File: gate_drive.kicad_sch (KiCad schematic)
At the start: 111 parts, among them U1 EG2131, U10 EG2131, U12 EG2131, U2 EG2131, U3 LM358, U4 EG2131, U5 EG2131, U8 LM358

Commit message: Updated PCB design based on feedback. Added thermistors, mounting holes. This design has better current carrying capacity. gerber folder may not be perfect right now.
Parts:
- removed C13: HIGHCURRENTPAD2, RP2040_minimal:PAD_12GA_WIRE, symbol Connector_Generic:Conn_01x01
- added M2C1: HIGHCURRENTPAD2, RP2040_minimal:PAD_12GA_WIRE, symbol Connector_Generic:Conn_01x01
- added TP1: TestPoint, symbol Connector:TestPoint
- R20, R22, R24, R26, R3, R4, R54, R55, R56, R57: value 22R -> 10.2R; LCSC C23345 -> C22773
- renumbered A1 to M1A1, B1 to M1B1, C12 to M1C1, A2 to M2A1, B2 to M2B1
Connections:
- net M2C: now also M2C1.1 (Pin_1)
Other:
- moved on the sheet: M2A1
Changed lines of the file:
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@@
     (stroke (width 0) (type default) (color 0 0 0 0))
   )
-  (wire (pts (xy 311.15 186.055) (xy 314.96 186.055))
+  (wire (pts (xy 311.15 186.055) (xy 316.23 186.055))
     (stroke (width 0) (type default) (color 0 0 0 0))
   )
@@
     (stroke (width 0) (type default) (color 0 0 0 0))
   )
-  (wire (pts (xy 120.015 182.88) (xy 123.825 182.88))
+  (wire (pts (xy 120.015 182.88) (xy 125.73 182.88))
     (stroke (width 0) (type default) (color 0 0 0 0))
   )
@@
     (pin "8")
   )
-  (symbol (lib_id "Connector_Generic:Conn_01x01") (at 128.905 182.88 0) (unit 1)
-    (in_bom no) (on_board yes)
-    (property "Reference" "C13" (id 0) (at 127.381 181.1274 0)
-      (effects (font (size 1.27 1.27)) (justify left bottom))
-    )
-    (property "Value" "HIGHCURRENTPAD2" (id 1) (at 128.651 185.674 0)
-      (effects (font (size 1.651 1.651)) (justify left top) hide)
-    )
-    (property "Footprint" "RP2040_minimal:PAD_12GA_WIRE" (id 2) (at 128.905 182.88 0)
-      (effects (font (size 1.27 1.27)) hide)
-    )
-    (property "Datasheet" "~" (id 3) (at 128.905 182.88 0)
-      (effects (font (size 1.27 1.27)) hide)
-    )
-    (pin "1")
-  )
   (symbol (lib_id "MotorController:TAYLOR_RESISTOR") (at 292.1 182.245 0) (unit 1)
     (in_bom yes) (on_board yes)
@@
       (effects (font (size 1.778 1.778)) (justify left bottom))
     )
-    (property "Value" "22R" (id 1) (at 288.29 185.547 0)
+    (property "Value" "10.2R" (id 1) (at 288.29 185.547 0)
       (effects (font (size 1.778 1.778)) (justify left bottom))
     )
@@
       (effects (font (size 1.27 1.27)) hide)
     )
-    (property "LCSC" "C23345" (id 4) (at 292.1 182.245 0)
+    (property "LCSC" "C22773" (id 4) (at 292.1 182.245 0)
       (effects (font (size 1.27 1.27)) hide)
     )
@@
   (symbol (lib_id "Connector_Generic:Conn_01x01") (at 211.455 57.15 0) (unit 1)
     (in_bom no) (on_board yes)
-    (property "Reference" "B1" (id 0) (at 209.931 55.3974 0)
+    (property "Reference" "M1B1" (id 0) (at 209.931 55.3974 0)
       (effects (font (size 1.27 1.27)) (justify left bottom))
     )
@@
     (pin "2")
   )
-  (symbol (lib_id "Connector_Generic:Conn_01x01") (at 320.04 186.055 0) (unit 1)
+  (symbol (lib_id "Connector_Generic:Conn_01x01") (at 321.31 186.055 0) (unit 1)
     (in_bom no) (on_board yes)
-    (property "Reference" "A2" (id 0) (at 318.516 184.3024 0)
+    (property "Reference" "M2A1" (id 0) (at 319.786 184.3024 0)
       (effects (font (size 1.27 1.27)) (justify left bottom))
     )
-    (property "Value" "HIGHCURRENTPAD2" (id 1) (at 319.786 188.849 0)
+    (property "Value" "HIGHCURRENTPAD2" (id 1) (at 321.056 188.849 0)
       (effects (font (size 1.651 1.651)) (justify left top) hide)
     )
-    (property "Footprint" "RP2040_minimal:PAD_12GA_WIRE" (id 2) (at 320.04 186.055 0)
+    (property "Footprint" "RP2040_minimal:PAD_12GA_WIRE" (id 2) (at 321.31 186.055 0)
       (effects (font (size 1.27 1.27)) hide)
     )
-    (property "Datasheet" "~" (id 3) (at 320.04 186.055 0)
+    (property "Datasheet" "~" (id 3) (at 321.31 186.055 0)
       (effects (font (size 1.27 1.27)) hide)
     )
@@
       (effects (font (size 1.778 1.778)) (justify left bottom))
     )
-    (property "Value" "22R" (id 1) (at 270.51 57.277 0)
+    (property "Value" "10.2R" (id 1) (at 270.51 57.277 0)
       (effects (font (size 1.778 1.778)) (justify left bottom))
     )
@@
       (effects (font (size 1.27 1.27)) hide)
     )
-    (property "LCSC" "C23345" (id 4) (at 274.32 53.975 0)
+    (property "LCSC" "C22773" (id 4) (at 274.32 53.975 0)
       (effects (font (size 1.27 1.27)) hide)
     )
@@
   (symbol (lib_id "Connector_Generic:Conn_01x01") (at 123.19 56.515 0) (unit 1)
     (in_bom no) (on_board yes)
-    (property "Reference" "C12" (id 0) (at 121.666 54.7624 0)
+    (property "Reference" "M1C1" (id 0) (at 121.666 54.7624 0)
       (effects (font (size 1.27 1.27)) (justify left bottom))
     )
@@
   (symbol (lib_id "Connector_Generic:Conn_01x01") (at 222.25 186.055 0) (unit 1)
     (in_bom no) (on_board yes)
-    (property "Reference" "B2" (id 0) (at 220.726 184.3024 0)
+    (property "Reference" "M2B1" (id 0) (at 220.726 184.3024 0)
       (effects (font (size 1.27 1.27)) (justify left bottom))
     )
@@
       (effects (font (size 1.778 1.778)) (justify left bottom))
     )
-    (property "Value" "22R" (id 1) (at 179.705 56.642 0)
+    (property "Value" "10.2R" (id 1) (at 179.705 56.642 0)
       (effects (font (size 1.778 1.778)) (justify left bottom))
     )
@@
       (effects (font (size 1.27 1.27)) hide)
     )
-    (property "LCSC" "C23345" (id 4) (at 183.515 53.34 0)
+    (property "LCSC" "C22773" (id 4) (at 183.515 53.34 0)
       (effects (font (size 1.27 1.27)) hide)
     )
@@
     (pin "2")
   )
+  (symbol (lib_id "Connector:TestPoint") (at -6.35 -104.14 0) (unit 1)
+    (in_bom yes) (on_board yes) (fields_autoplaced)
+    (property "Reference" "TP1" (id 0) (at -2.54 -108.7121 0)
+      (effects (font (size 1.27 1.27)) (justify left))
+    )
+    (property "Value" "TestPoint" (id 1) (at -2.54 -106.1721 0)
+      (effects (font (size 1.27 1.27)) (justify left))
+    )
+    (property "Footprint" "" (id 2) (at -1.27 -104.14 0)
+      (effects (font (size 1.27 1.27)) hide)
+    )
+    (property "Datasheet" "~" (id 3) (at -1.27 -104.14 0)
+      (effects (font (size 1.27 1.27)) hide)
+    )
+    (pin "1")
+  )
   (symbol (lib_id "Device:D") (at 185.42 164.465 180) (unit 1)
     (in_bom yes) (on_board yes) (fields_autoplaced)
@@
       (effects (font (size 1.778 1.778)) (justify left bottom))
     )
-    (property "Value" "22R" (id 1) (at 97.155 182.372 0)
+    (property "Value" "10.2R" (id 1) (at 97.155 182.372 0)
       (effects (font (size 1.778 1.778)) (justify left bottom))
     )
@@
       (effects (font (size 1.27 1.27)) hide)
     )
-    (property "LCSC" "C23345" (id 4) (at 100.965 179.07 0)
+    (property "LCSC" "C22773" (id 4) (at 100.965 179.07 0)
       (effects (font (size 1.27 1.27)) hide)
     )
@@
   (symbol (lib_id "Connector_Generic:Conn_01x01") (at 302.26 57.785 0) (unit 1)
     (in_bom no) (on_board yes)
-    (property "Reference" "A1" (id 0) (at 300.736 56.0324 0)
+    (property "Reference" "M1A1" (id 0) (at 300.736 56.0324 0)
       (effects (font (size 1.27 1.27)) (justify left bottom))
     )
@@
       (effects (font (size 1.778 1.778)) (justify left bottom))
     )
-    (property "Value" "22R" (id 1) (at 270.51 71.247 0)
+    (property "Value" "10.2R" (id 1) (at 270.51 71.247 0)
       (effects (font (size 1.778 1.778)) (justify left bottom))
     )
@@
       (effects (font (size 1.27 1.27)) hide)
     )
-    (property "LCSC" "C23345" (id 4) (at 274.32 67.945 0)
+    (property "LCSC" "C22773" (id 4) (at 274.32 67.945 0)
       (effects (font (size 1.27 1.27)) hide)
     )
@@
       (effects (font (size 1.778 1.778)) (justify left bottom))
     )
-    (property "Value" "22R" (id 1) (at 288.29 199.517 0)
+    (property "Value" "10.2R" (id 1) (at 288.29 199.517 0)
       (effects (font (size 1.778 1.778)) (justify left bottom))
     )
@@
       (effects (font (size 1.27 1.27)) hide)
     )
-    (property "LCSC" "C23345" (id 4) (at 292.1 196.215 0)
+    (property "LCSC" "C22773" (id 4) (at 292.1 196.215 0)
       (effects (font (size 1.27 1.27)) hide)
     )
@@
       (effects (font (size 1.778 1.778)) (justify left bottom))
     )
-    (property "Value" "22R" (id 1) (at 190.5 199.517 0)
+    (property "Value" "10.2R" (id 1) (at 190.5 199.517 0)
       (effects (font (size 1.778 1.778)) (justify left bottom))
     )
@@
       (effects (font (size 1.27 1.27)) hide)
     )
-    (property "LCSC" "C23345" (id 4) (at 194.31 196.215 0)
+    (property "LCSC" "C22773" (id 4) (at 194.31 196.215 0)
       (effects (font (size 1.27 1.27)) hide)
     )
@@
       (effects (font (size 1.778 1.778)) (justify left bottom))
     )
-    (property "Value" "22R" (id 1) (at 97.155 196.342 0)
+    (property "Value" "10.2R" (id 1) (at 97.155 196.342 0)
       (effects (font (size 1.778 1.778)) (justify left bottom))
     )
@@
       (effects (font (size 1.27 1.27)) hide)
     )
-    (property "LCSC" "C23345" (id 4) (at 100.965 193.04 0)
+    (property "LCSC" "C22773" (id 4) (at 100.965 193.04 0)
       (effects (font (size 1.27 1.27)) hide)
     )
@@
       (effects (font (size 1.778 1.778)) (justify left bottom))
     )
-    (property "Value" "22R" (id 1) (at 190.5 185.547 0)
+    (property "Value" "10.2R" (id 1) (at 190.5 185.547 0)
       (effects (font (size 1.778 1.778)) (justify left bottom))
     )
@@
       (effects (font (size 1.27 1.27)) hide)
     )
-    (property "LCSC" "C23345" (id 4) (at 194.31 182.245 0)
+    (property "LCSC" "C22773" (id 4) (at 194.31 182.245 0)
       (effects (font (size 1.27 1.27)) hide)
     )
@@
       (effects (font (size 1.778 1.778)) (justify left bottom))
     )
-    (property "Value" "22R" (id 1) (at 179.705 70.612 0)
+    (property "Value" "10.2R" (id 1) (at 179.705 70.612 0)
       (effects (font (size 1.778 1.778)) (justify left bottom))
     )
@@
       (effects (font (size 1.27 1.27)) hide)
     )
-    (property "LCSC" "C23345" (id 4) (at 183.515 67.31 0)
+    (property "LCSC" "C22773" (id 4) (at 183.515 67.31 0)
       (effects (font (size 1.27 1.27)) hide)
     )
@@
     (pin "8")
   )
+  (symbol (lib_id "Connector_Generic:Conn_01x01") (at 130.81 182.88 0) (unit 1)
+    (in_bom no) (on_board yes)
+    (property "Reference" "M2C1" (id 0) (at 129.286 181.1274 0)
+      (effects (font (size 1.27 1.27)) (justify left bottom))
+    )
+    (property "Value" "HIGHCURRENTPAD2" (id 1) (at 130.556 185.674 0)
+      (effects (font (size 1.651 1.651)) (justify left top) hide)
+    )
+    (property "Footprint" "RP2040_minimal:PAD_12GA_WIRE" (id 2) (at 130.81 182.88 0)
+      (effects (font (size 1.27 1.27)) hide)
+    )
+    (property "Datasheet" "~" (id 3) (at 130.81 182.88 0)
+      (effects (font (size 1.27 1.27)) hide)
+    )
+    (pin "1")
+  )
 )

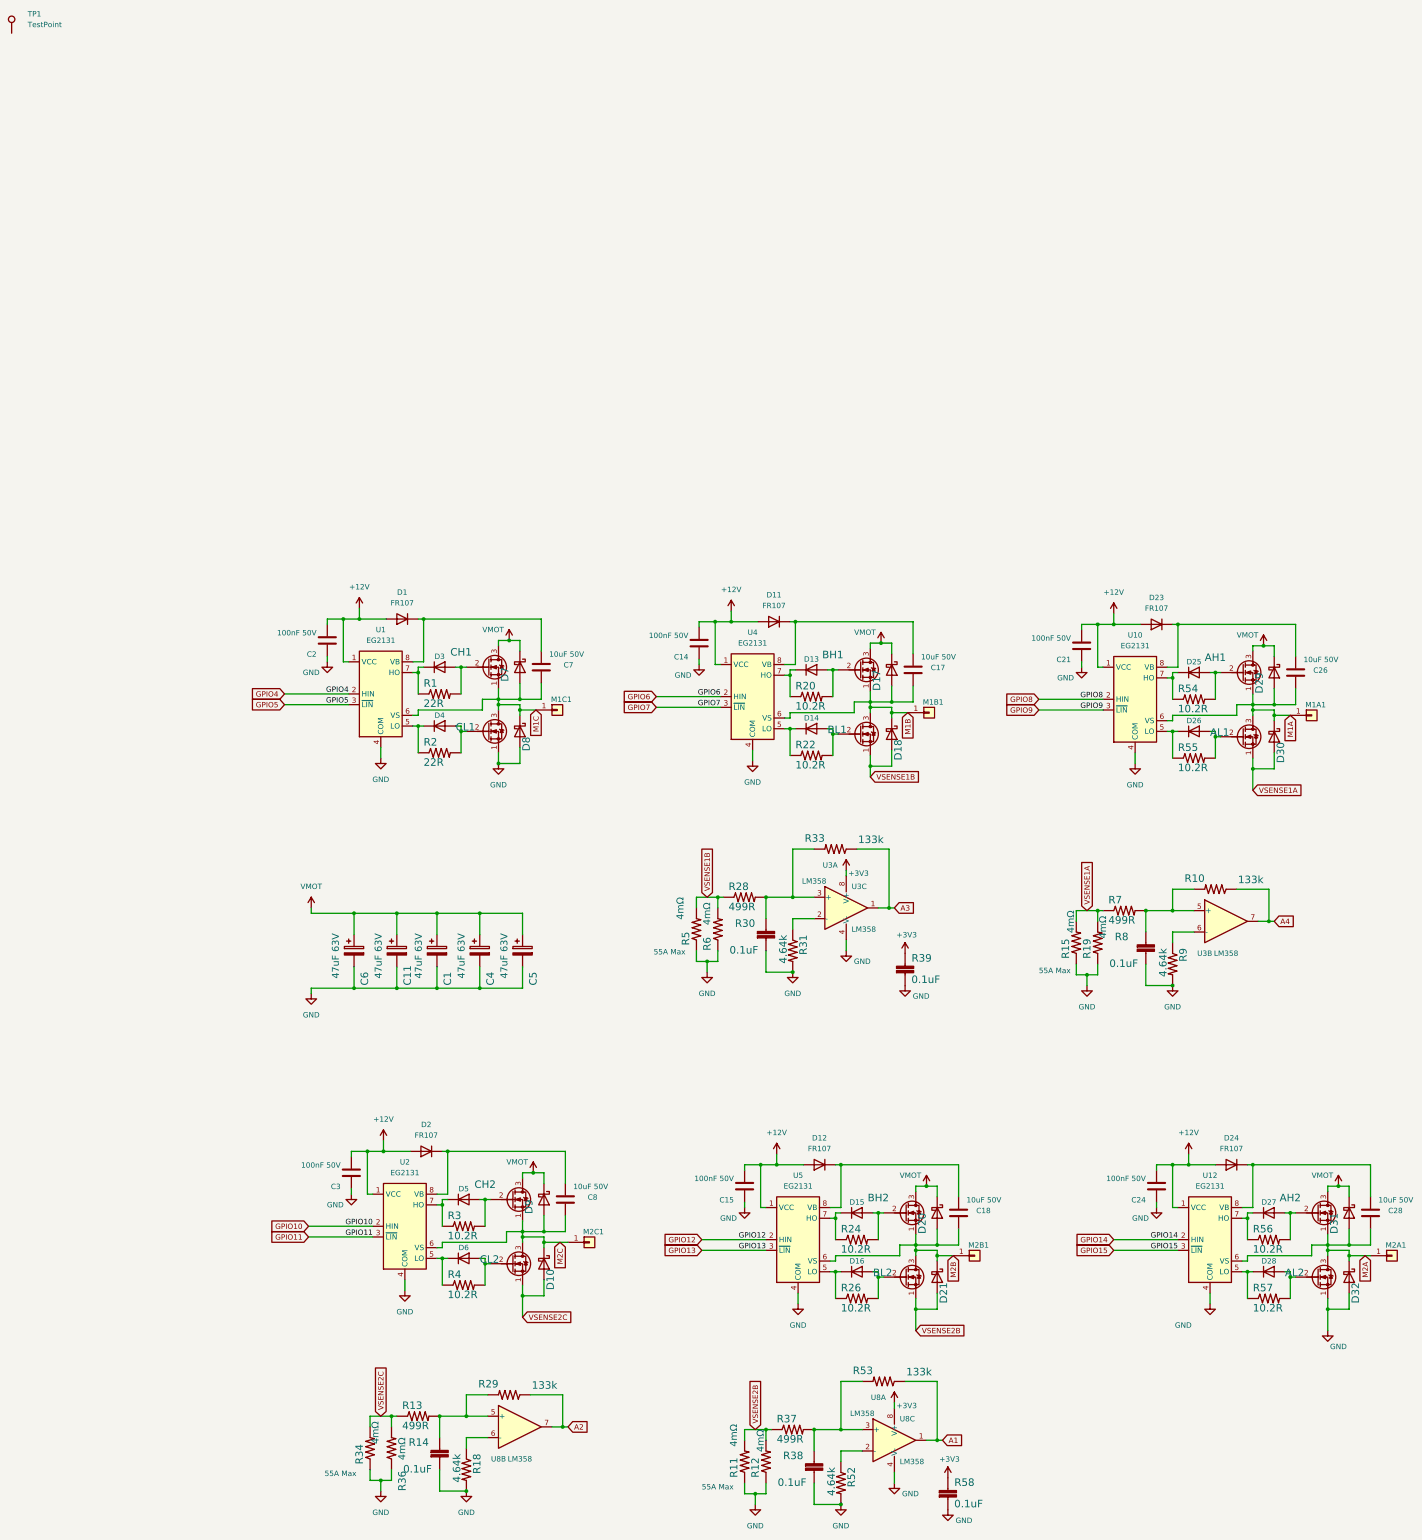
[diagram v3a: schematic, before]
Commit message: Additional updates to clean up power and capacitance on buck circuit.
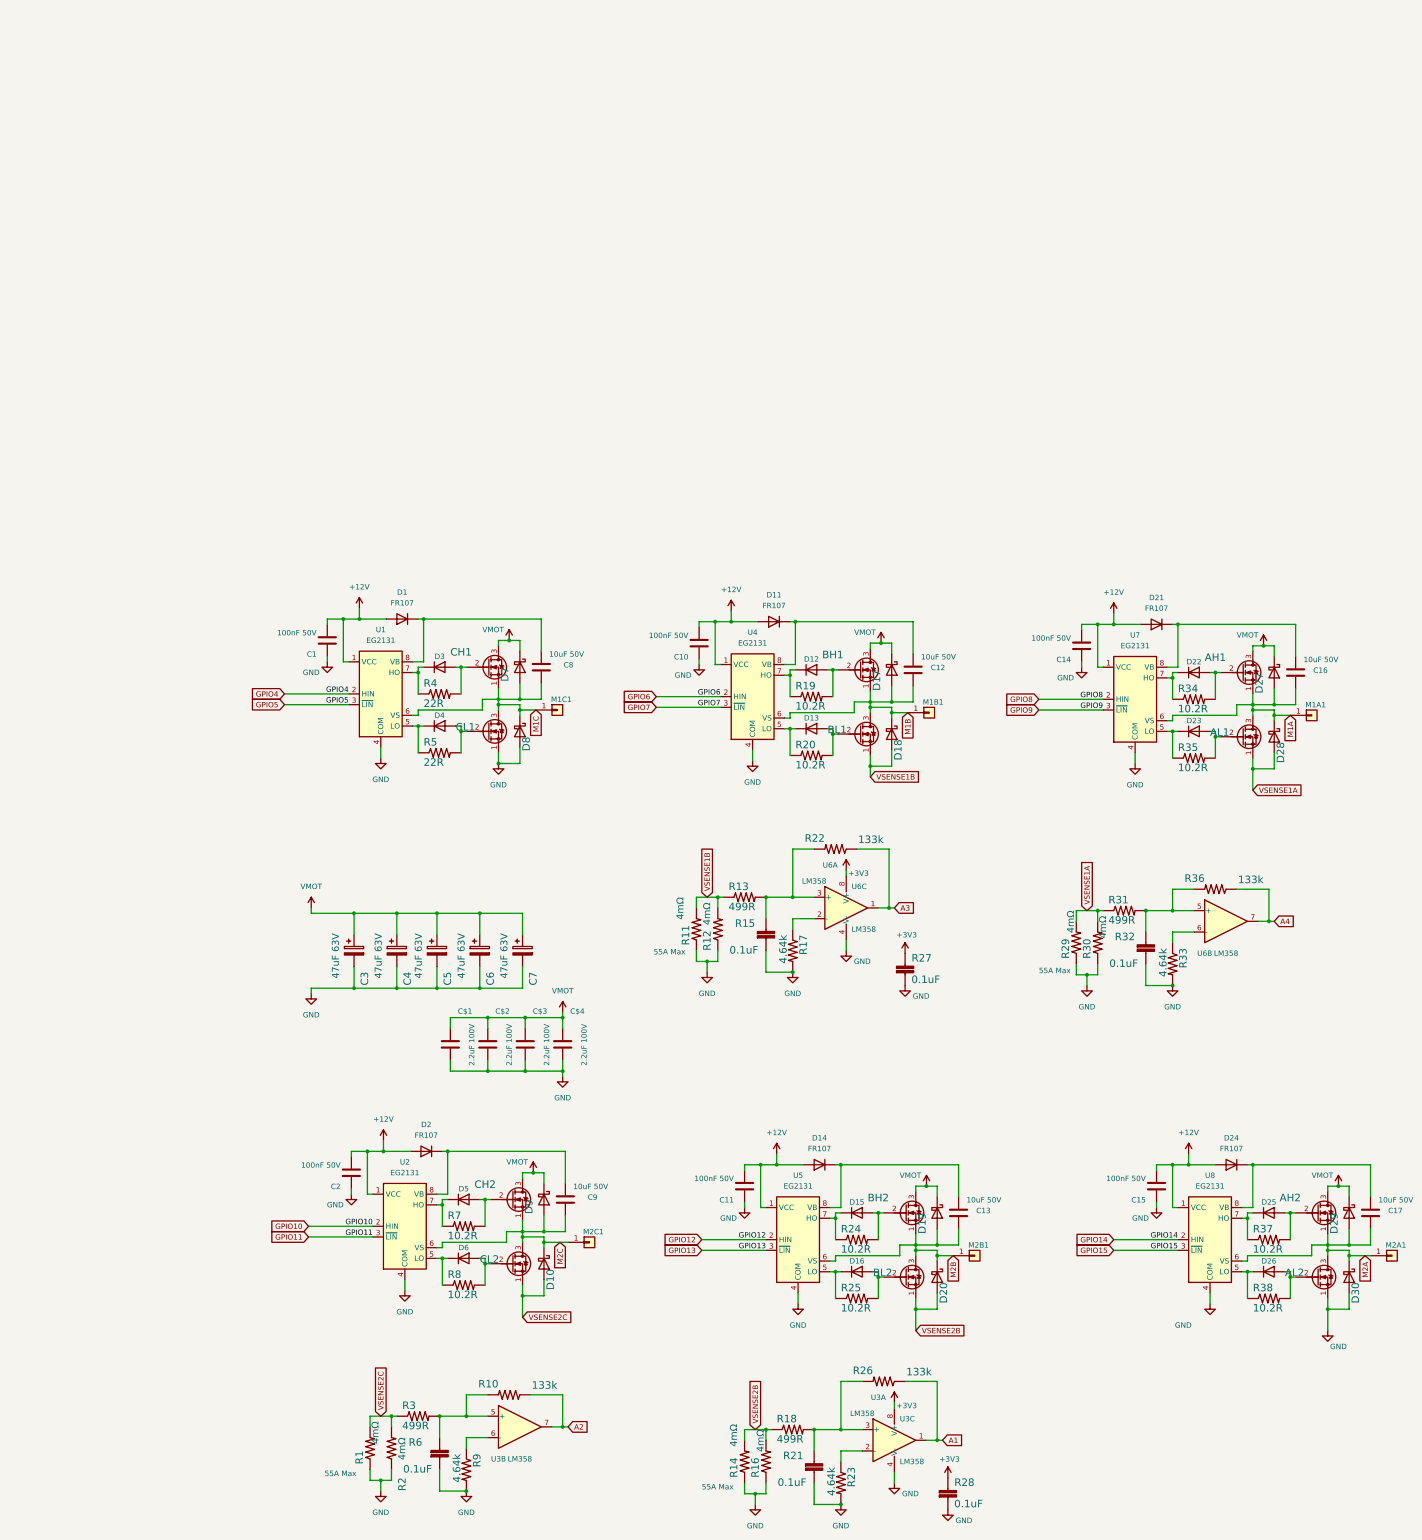
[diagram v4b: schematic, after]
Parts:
- removed TP1: TestPoint, symbol Connector:TestPoint
- added C$1, C$2, C$3, C$4: 2.2uF 100V, Capacitor_SMD:C_1206_3216Metric, symbol Device:C
- renumbered C2 to C1, C14 to C10, C15 to C11, C17 to C12, C18 to C13, C21 to C14, C24 to C15, C26 to C16, C28 to C17, C3 to C2, C6 to C3, C11 to C4, C1 to C5, C4 to C6, C5 to C7, C7 to C8, C8 to C9, D13 to D12, D14 to D13, D12 to D14, D20 to D19, D21 to D20, D23 to D21, D25 to D22, D26 to D23, D27 to D25, D28 to D26, D29 to D27, D30 to D28, D31 to D29, D32 to D30, R34 to R1, R29 to R10, R5 to R11, R6 to R12, R28 to R13, R11 to R14, R30 to R15, R12 to R16, R31 to R17, R37 to R18, R20 to R19, R36 to R2, R22 to R20, R38 to R21, R33 to R22, R52 to R23, R26 to R25, R53 to R26, R39 to R27, R58 to R28, R15 to R29, R13 to R3, R19 to R30, R7 to R31, R8 to R32, R9 to R33, R54 to R34, R55 to R35, R10 to R36, R56 to R37, R57 to R38, R1 to R4, R2 to R5, R14 to R6, R3 to R7, R4 to R8, R18 to R9, U8 to U3, U3 to U6, U10 to U7, U12 to U8
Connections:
- net GND: now also C$1.2, C$2.2, C$3.2, C$4.2
- net VMOT: now also C$1.1, C$2.1, C$3.1, C$4.1
